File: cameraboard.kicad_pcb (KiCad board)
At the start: 2 copper layers, 44.4 x 35.8 mm, 8 parts, among them J1 Conn_02x05_Odd_Even, Q1 Nikla_Vision, Q2 SSM3J133TU,LF

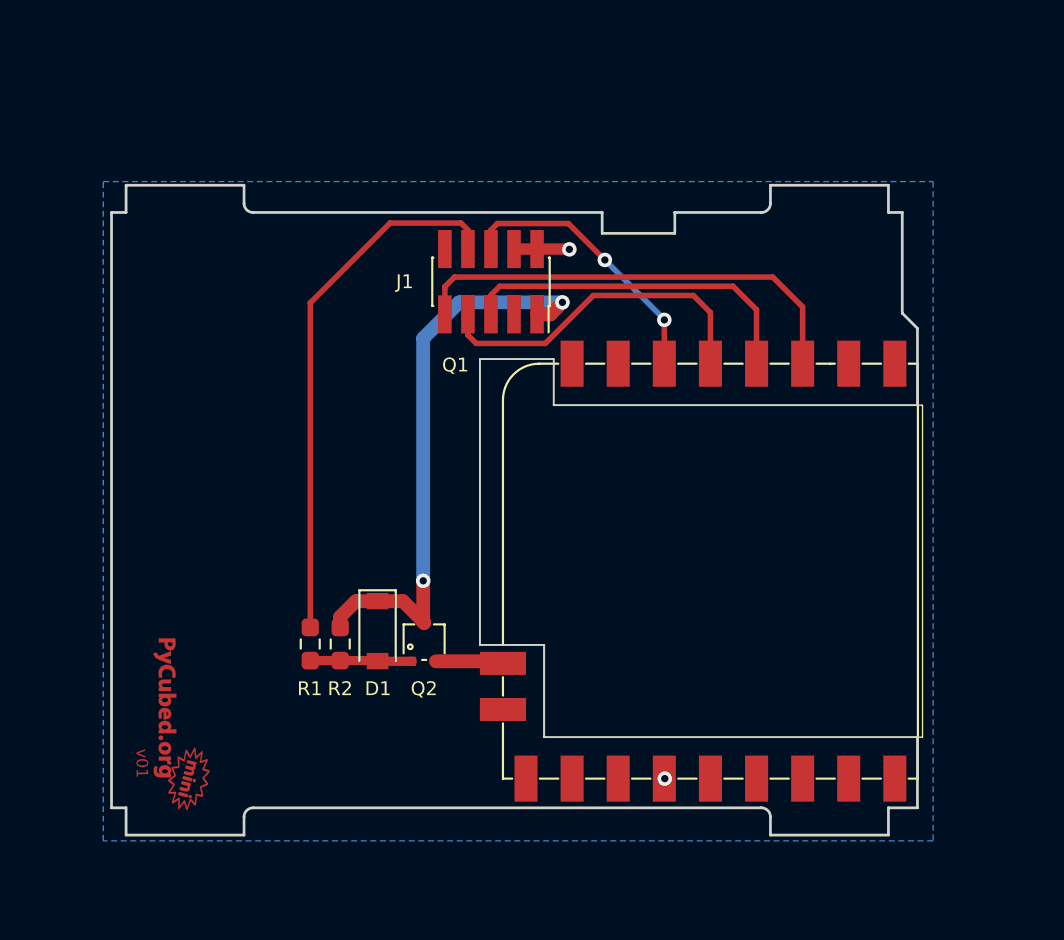
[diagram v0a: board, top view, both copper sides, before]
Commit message: Changed board shape and rewired
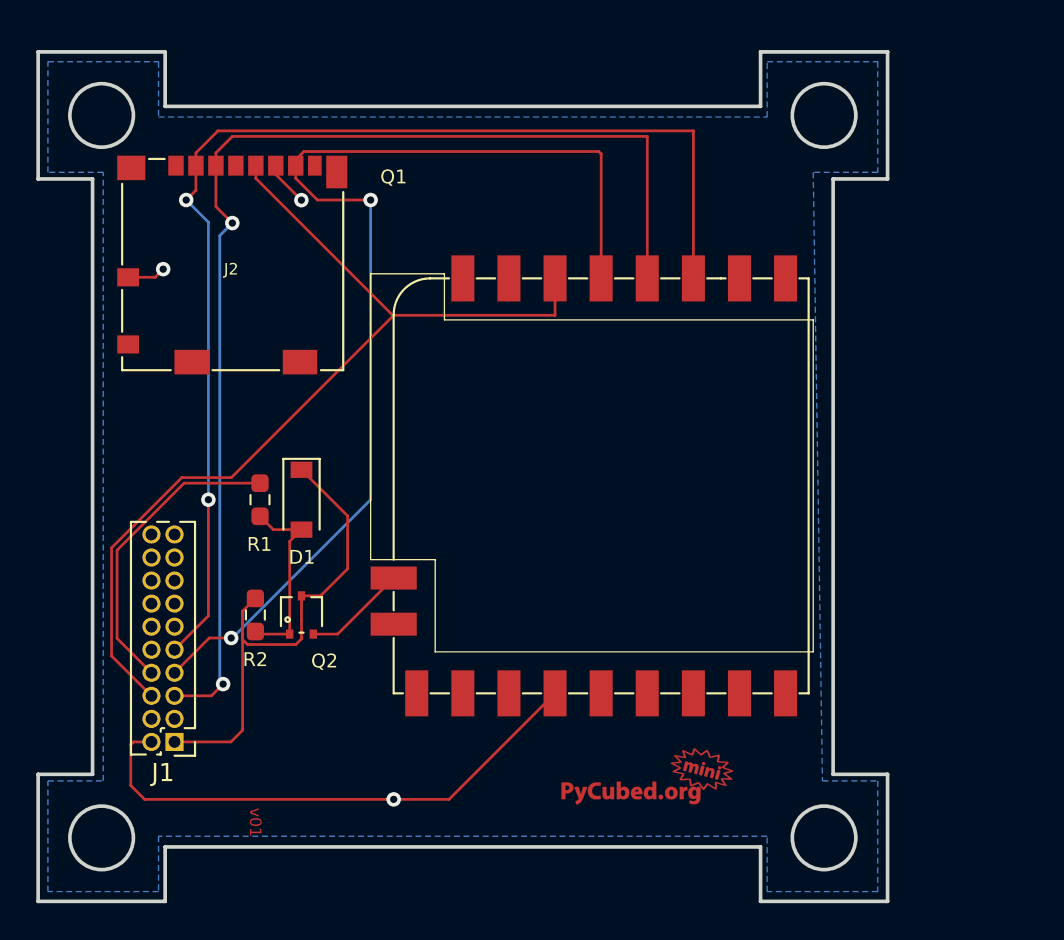
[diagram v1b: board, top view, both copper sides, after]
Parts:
- added J2: Micro_SD_Card, cameraboard:microSD_HC_Molex_104031-0811, F.Cu at (86.4, 49.3)
- J1: value Conn_02x05_Odd_Even -> Conn_02x10_Odd_Even; footprint Connector_PinSocket_1.27mm:PinSocket_2x05_P1.27mm_Vertical_SMD -> Connector_PinHeader_1.27mm:PinHeader_2x10_P1.27mm_Vertical
- moved J1 30.8 mm to (83.2, 75.6), turned to 180 degrees
- moved Ref** 25.8 mm to (109.2, 77.5), turned to 0 degrees (x2)
- moved R1 8.42 mm to (87.9, 62.2)
- moved D1 8.36 mm to (90.2, 62.2)
- moved Q1 7.64 mm to (106.7, 61.5)
- moved Q2 6.92 mm to (90.2, 68.6)
- moved R2 4.94 mm to (87.6, 68.6)
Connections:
- net /CAM_CS renamed CS
- net /CAM_EN renamed /EN
- net /CAM_MISO renamed MISO
- net /CAM_MOSI renamed MOSI
- net /CAM_SCLK renamed SCLK
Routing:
- net MOSI: track 19.4 -> 64.9 mm, vias 0 -> 2
- net MISO: track 19.0 -> 60.8 mm, vias 0 -> 2
- net CS: track 25.3 -> 64.9 mm, vias 0 -> 2
- net SCLK: track 15.4 -> 52.3 mm, vias 2 -> 0
- net GND: track 3.06 -> 34.2 mm, vias 2 -> 3
- net /EN: track 29.6 -> 16.9 mm
- net Net-(D1-Pad2): track 5.64 -> 10.6 mm
- net /BATT_P: track 32.0 -> 28.7 mm, vias 2 -> 0
- net Net-(Q1-PadC2): track 3.74 -> 5.71 mm
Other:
- board size 44.4 x 35.8 mm -> 46.8 x 46.8 mm

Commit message: Schematic fixes and re-routing
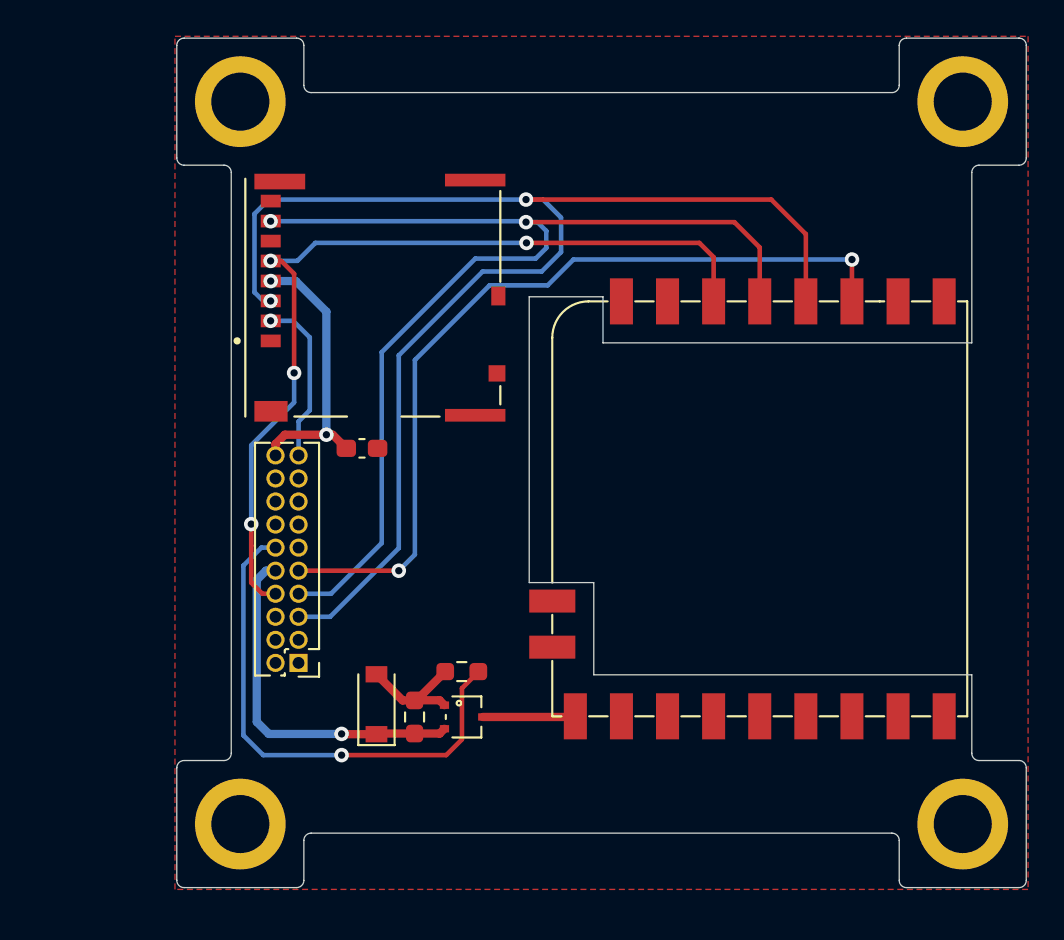
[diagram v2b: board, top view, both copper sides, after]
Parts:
- removed the Ref** at (109.2, 77.5)
- added C1: 1uF, Capacitor_SMD:C_0603_1608Metric_Pad1.08x0.95mm_HandSolder, F.Cu at (93.5, 59.4)
- added H1: MountingHole_Pad, mainboard:MountingHole, F.Cu at (86.8, 40.3)
- added H2: MountingHole_Pad, mainboard:MountingHole, F.Cu at (126.6, 40.3)
- added H3: MountingHole_Pad, mainboard:MountingHole, F.Cu at (126.6, 80.1)
- added H4: MountingHole_Pad, mainboard:MountingHole, F.Cu at (86.8, 80.1)
- J1: value Conn_02x10_Odd_Even -> 02x10 1.27mm
- J2: footprint cameraboard:microSD_HC_Molex_104031-0811 -> cameraboard:MOLEX_503398-1892
- moved Ref** 36.3 mm to (118.0, 42.2)
- moved R1 14.6 mm to (99.0, 71.7), turned to 180 degrees
- moved D1 12.0 mm to (94.3, 73.5), turned to 90 degrees
- moved Q2 10.6 mm to (99.1, 74.2), turned to -90 degrees
- moved R2 10.4 mm to (96.4, 74.2), turned to 90 degrees
- moved Q1 8.83 mm to (115.4, 62.7)
- moved J1 8.10 mm to (90.0, 71.2)
- moved J2 7.95 mm to (94.1, 51.1), turned to 90 degrees
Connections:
- net MISO renamed /MISO
- net MOSI renamed /MOSI
- D1 pad 1: /BATT_P -> HI_POW
- J1 pad 1: /BATT_P -> unconnected-(J1-Pad1)
- J1 pad 10: unconnected-(J1-Pad10) -> HI_POW
- J1 pad 12: unconnected-(J1-Pad12) -> /CAM_EN
- J1 pad 19: unconnected-(J1-Pad19) -> /SD_CS
- J1 pad 2: GND -> unconnected-(J1-Pad2)
- J1 pad 20: unconnected-(J1-Pad20) -> +3V3
- J1 pad 6: SCLK -> GND
- J1 pad 8: /EN -> /SCK
- J1 pad 9: CS -> /CAM_CS
- J2 pad 2: CS -> /SD_CS
- J2 pad 5: SCLK -> /SCK
- Q1 pad A3: CS -> /CAM_CS
- Q1 pad A6: SCLK -> /SCK
- Q1 pad B9: unconnected-(Q1-PadB9) -> Net-(Q1-PadB9)
- Q1 pad C2: Net-(Q1-PadC2) -> unconnected-(Q1-PadC2)
- Q2 pad 2: Net-(Q1-PadC2) -> HI_POW
- Q2 pad 3: /BATT_P -> Net-(Q1-PadB9)
- R1 pad 1: /EN -> /CAM_EN
- R2 pad 1: /BATT_P -> HI_POW
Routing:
- net CS: track 64.9 -> 0.00 mm, vias 2 -> 0
- net SCLK: track 52.3 -> 0.00 mm
- net /SCK: track 0.00 -> 48.8 mm, vias 0 -> 4
- net /CAM_CS: track 0.00 -> 46.2 mm, vias 0 -> 2
- net GND: track 34.2 -> 0.00 mm, vias 3 -> 0
- net /BATT_P: track 28.7 -> 0.00 mm
- net /CAM_EN: track 0.00 -> 28.5 mm, vias 0 -> 1
- net HI_POW: track 0.00 -> 19.8 mm, vias 0 -> 1
- net /EN: track 16.9 -> 0.00 mm
- net +3V3: track 0.00 -> 15.6 mm, vias 0 -> 2
- net /SD_CS: track 0.00 -> 9.30 mm, vias 0 -> 1
- net /MOSI: track 64.9 -> 73.9 mm
- net Net-(Q1-PadC2): track 5.71 -> 0.00 mm
- net Net-(Q1-PadB9): track 0.00 -> 5.12 mm
- net Net-(D1-Pad2): track 10.6 -> 6.80 mm
- added copper zone on F.Cu, net GND
- removed copper zone on B.Cu, net GND
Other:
- outline, holes or cut-outs redrawn
- board text added: "v02"
- board text removed: "v01"

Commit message: Moved stuff into place
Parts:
- moved Ref** 26.9 mm to (100.9, 62.9), turned to -90 degrees
- moved C1 13.8 mm to (88.8, 46.4), turned to -90 degrees
- moved J2 4.68 mm to (97.2, 47.6), turned to 0 degrees
- moved J1 3.00 mm to (90.0, 68.2)
- moved Q1 1.90 mm to (117.3, 62.7)
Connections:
- J1 pad 10: HI_POW -> /CAM_EN
- J1 pad 12: /CAM_EN -> /SCK
- J1 pad 8: /SCK -> HI_POW
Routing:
- net /MOSI: track 73.9 -> 57.9 mm
- net /SD_CS: track 9.30 -> 17.3 mm
- net /MISO: track 60.5 -> 54.4 mm, vias 2 -> 3
- net +3V3: track 15.6 -> 21.7 mm, vias 2 -> 0
- net /SCK: track 48.8 -> 52.2 mm, vias 4 -> 2
- net Net-(Q1-PadB9): track 5.12 -> 7.03 mm
- net /CAM_CS: track 46.2 -> 47.2 mm
- net HI_POW: track 19.8 -> 20.5 mm
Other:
- outline, holes or cut-outs redrawn

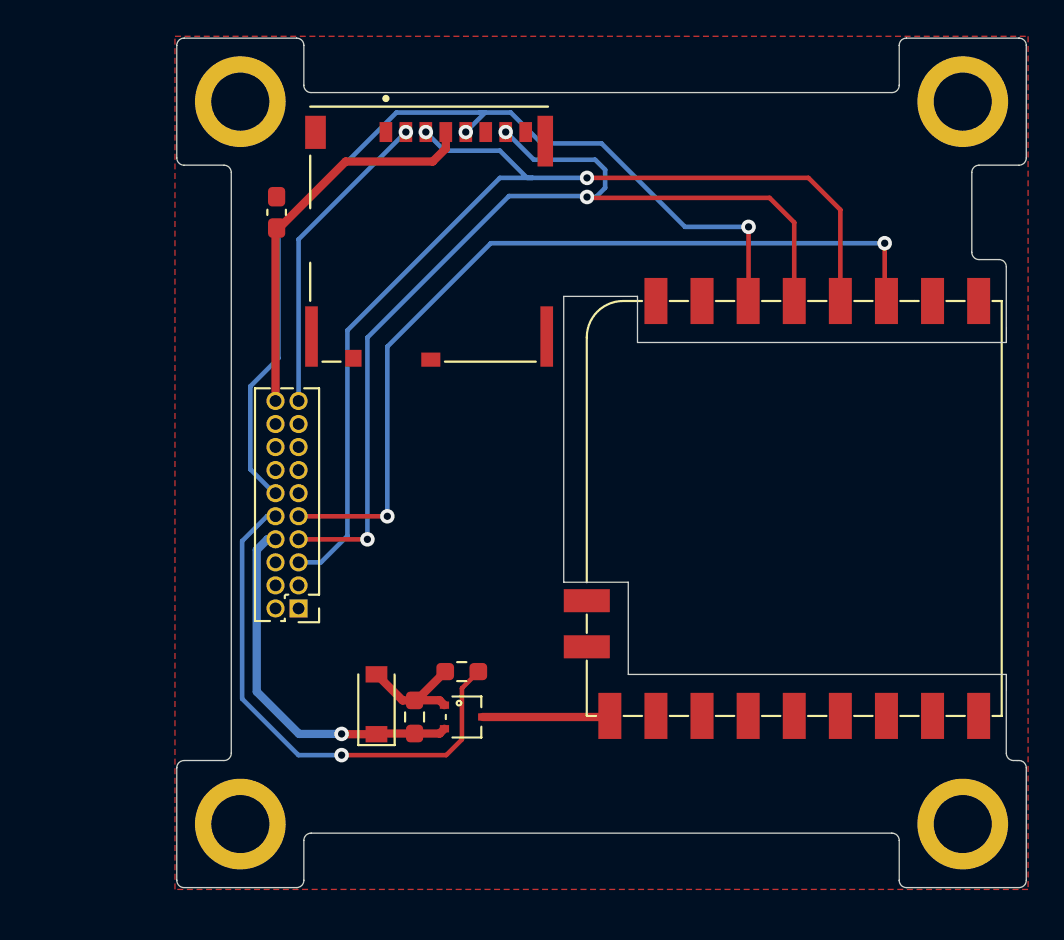
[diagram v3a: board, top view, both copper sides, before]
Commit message: stack connectors changes
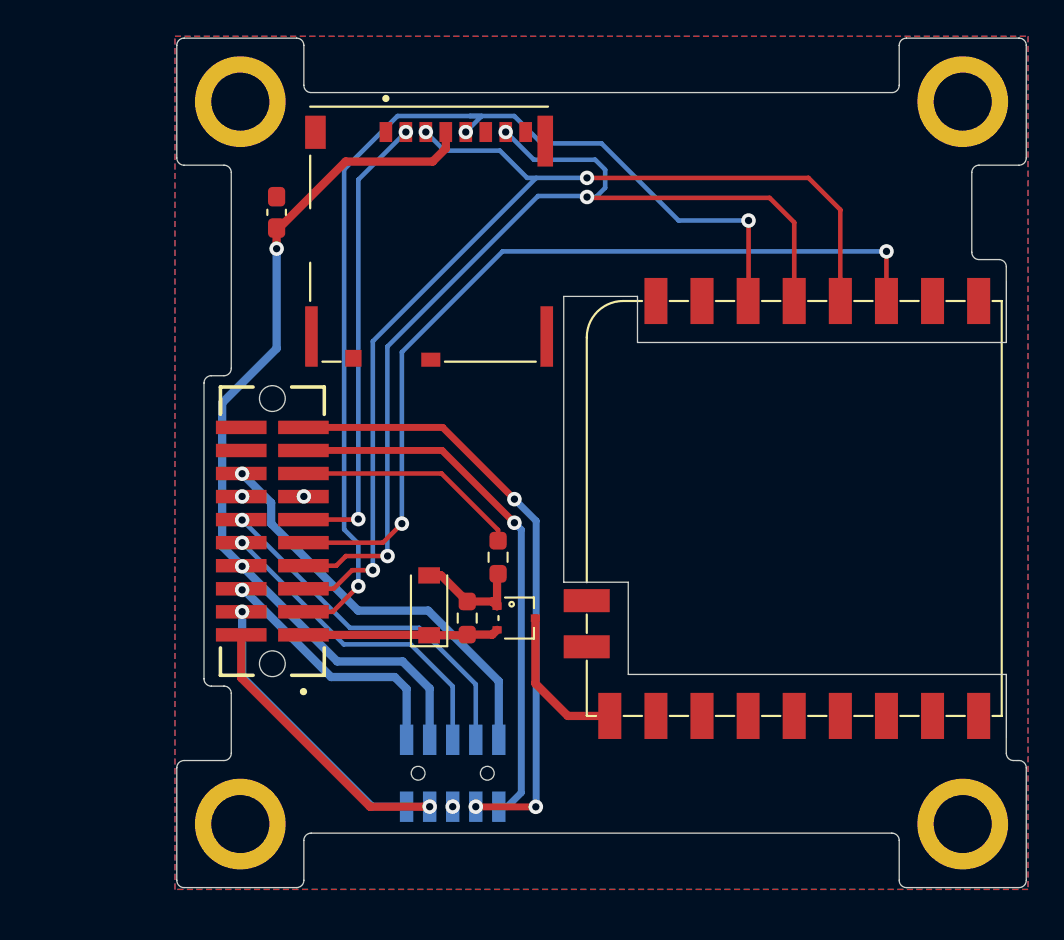
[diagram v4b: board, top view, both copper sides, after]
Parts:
- added J3: Conn 01x10 1.27mm, cameraboard:SAMTEC_FLE-105-01-G-DV-A, B.Cu at (98.5, 77.3)
- J1: footprint Connector_PinHeader_1.27mm:PinHeader_2x10_P1.27mm_Vertical -> cameraboard:SAMTEC_TFM-110-12-L-D-A
- moved Ref** 27.4 mm to (118.6, 42.0), turned to 0 degrees
- moved R1 6.61 mm to (101.0, 65.4), turned to -90 degrees
- moved D1 6.17 mm to (97.2, 68.0)
- moved Q2 6.17 mm to (102.0, 68.7)
- moved R2 6.17 mm to (99.3, 68.7)
- moved J1 4.50 mm to (88.6, 64.0), turned to 90 degrees
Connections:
- J1 pad 1: unconnected-(J1-Pad1) -> HI_POW
- J1 pad 10: /CAM_EN -> SCL3
- J1 pad 11: unconnected-(J1-Pad11) -> /SD_CS
- J1 pad 12: /SCK -> SDA3
- J1 pad 13: unconnected-(J1-Pad13) -> GND
- J1 pad 14: unconnected-(J1-Pad14) -> GND
- J1 pad 15: unconnected-(J1-Pad15) -> /CAM_EN
- J1 pad 16: unconnected-(J1-Pad16) -> VBUS
- J1 pad 17: unconnected-(J1-Pad17) -> COIL6_N
- J1 pad 19: /SD_CS -> COIL6_P
- J1 pad 2: unconnected-(J1-Pad2) -> BATT_P
- J1 pad 20: +3V3 -> unconnected-(J1-Pad20)
- J1 pad 3: unconnected-(J1-Pad3) -> /SCK
- J1 pad 4: GND -> BATT_N_SW
- J1 pad 6: GND -> BATT_P_SW
- J1 pad 8: HI_POW -> +3V3
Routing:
- net COIL6_P: track 0.00 -> 34.0 mm, vias 0 -> 3
- net COIL6_N: track 0.00 -> 29.9 mm, vias 0 -> 1
- net +3V3: track 21.7 -> 48.0 mm, vias 0 -> 2
- net VBUS: track 0.00 -> 22.8 mm, vias 0 -> 1
- net SDA3: track 0.00 -> 19.7 mm, vias 0 -> 1
- net SCL3: track 0.00 -> 17.8 mm, vias 0 -> 1
- net /CAM_EN: track 29.0 -> 12.6 mm, vias 1 -> 0
- net BATT_P: track 0.00 -> 15.7 mm, vias 0 -> 1
- net BATT_N_SW: track 0.00 -> 15.6 mm, vias 0 -> 1
- net BATT_P_SW: track 0.00 -> 14.1 mm, vias 0 -> 1
- net HI_POW: track 20.5 -> 10.7 mm, vias 1 -> 0
- net /SD_CS: track 17.3 -> 25.4 mm, vias 1 -> 2
- net /SCK: track 52.2 -> 58.5 mm, vias 2 -> 3
- net Net-(Q1-PadB9): track 7.03 -> 8.45 mm
- net /MOSI: track 57.9 -> 59.2 mm, vias 2 -> 3
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- added copper zone on B.Cu, net GND
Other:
- outline, holes or cut-outs redrawn

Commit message: VBUS -> VUSB
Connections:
- net VBUS renamed VUSB
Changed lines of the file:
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@@
   (net 28 "SCL3")
   (net 29 "SDA3")
-  (net 30 "VBUS")
+  (net 30 "VUSB")
   (net 31 "COIL6_N")
   (net 32 "COIL6_P")
@@
       (net 21 "/CAM_EN") (pinfunction "Pin_15") (pintype "passive"))
     (pad "16" smd rect (at 3.175 -1.715 90) (size 0.74 2.79) (layers "F.Cu" "F.Paste" "F.Mask")
-      (net 30 "VBUS") (pinfunction "Pin_16") (pintype "passive"))
+      (net 30 "VUSB") (pinfunction "Pin_16") (pintype "passive"))
     (pad "17" smd rect (at 4.445 1.715 90) (size 0.74 2.79) (layers "F.Cu" "F.Paste" "F.Mask")
       (net 31 "COIL6_N") (pinfunction "Pin_17") (pintype "passive"))
@@
       (net 31 "COIL6_N") (pinfunction "Pin_9") (pintype "passive"))
     (pad "10" smd rect (at 2.54 -1.8425) (size 0.74 1.675) (layers "B.Cu" "B.Paste" "B.Mask")
-      (net 30 "VBUS") (pinfunction "Pin_10") (pintype "passive"))
+      (net 30 "VUSB") (pinfunction "Pin_10") (pintype "passive"))
     (model "${KIPRJMOD}/kicad-libs/3d/FLE-105-01-G-DV-A.step" hide
       (offset (xyz 0 0 0.1524))
